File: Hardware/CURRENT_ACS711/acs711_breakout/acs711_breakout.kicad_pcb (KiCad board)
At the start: 2 copper layers, 40 x 30 mm, 13 parts, among them J1 Conn_01x01, J2 Conn_01x01, J3 Conn_01x04, U1 ACS711xEXLT-15AB

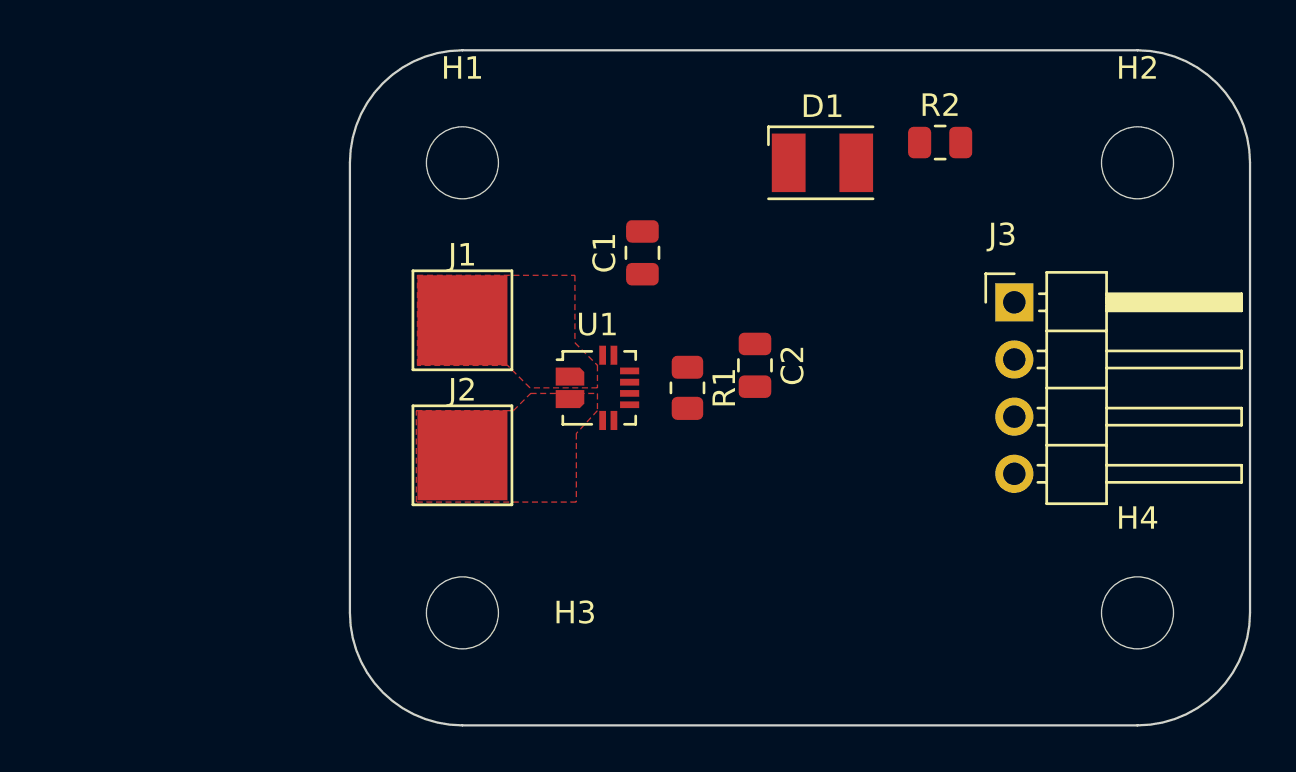
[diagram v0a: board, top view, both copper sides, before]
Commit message: layout and some stitching vias
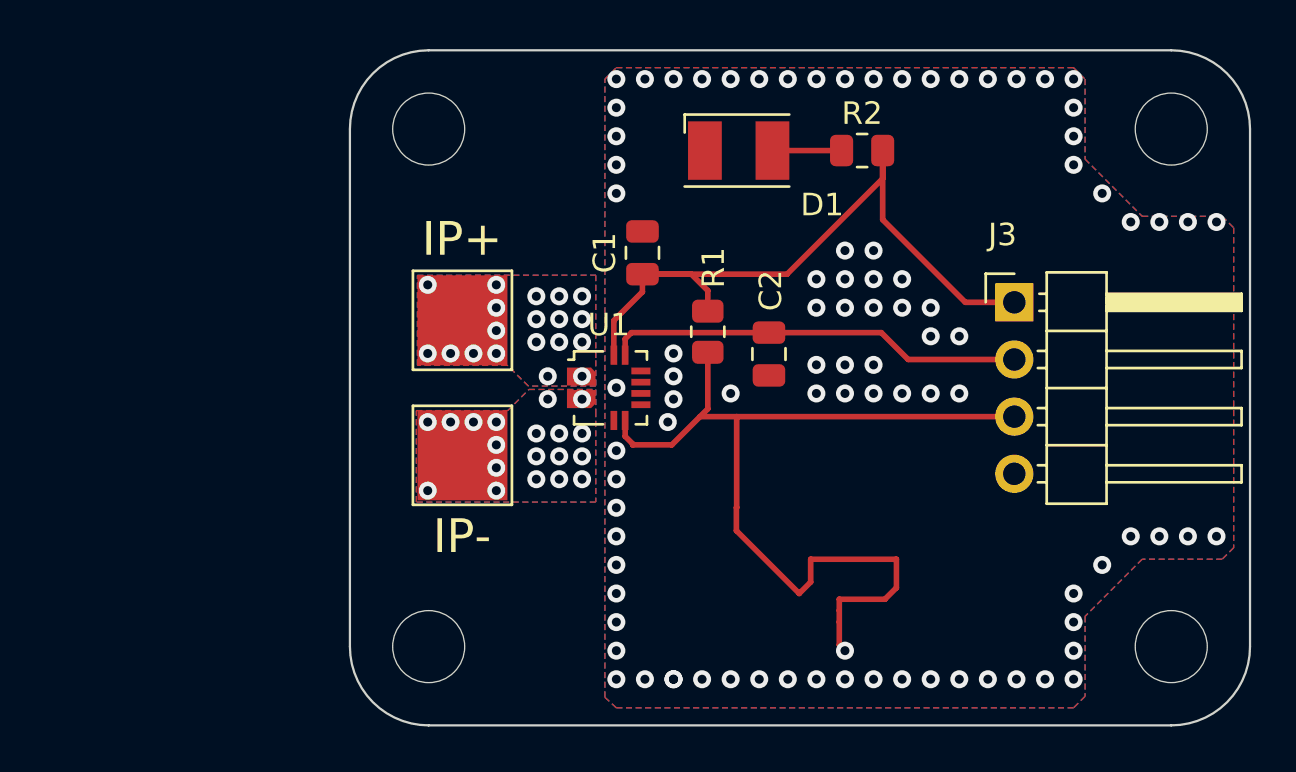
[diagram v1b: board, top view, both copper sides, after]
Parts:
- moved D1 3.76 mm to (122.3, 84.5)
- moved R2 3.49 mm to (127.8, 84.5)
- moved R1 2.65 mm to (120.9, 92.5)
- moved H1 2.12 mm to (108.5, 83.5)
- moved H2 2.12 mm to (141.5, 83.5)
- moved H3 2.12 mm to (108.5, 106.5)
- moved H4 2.12 mm to (141.5, 106.5)
- moved C2 0.80 mm to (123.6, 93.5)
- moved U1 0.50 mm to (116.5, 95.0)
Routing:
- net Net-(J3-Pad3): track 0.00 -> 42.7 mm, vias 0 -> 1
- net VCC: track 0.00 -> 32.4 mm
- net Net-(C2-Pad1): track 0.00 -> 18.6 mm
- net Net-(D1-Pad2): track 0.00 -> 3.07 mm
- net Net-(J2-Pad1): vias 0 -> 19
- net Net-(J1-Pad1): vias 0 -> 19
- net GND: vias 0 -> 91
- added copper zone on B.Cu, net GND
- added copper zone on F.Cu, net GND
- added copper zone on B.Cu, net Net-(J1-Pad1)
- added copper zone on B.Cu, net Net-(J2-Pad1)
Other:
- outline, holes or cut-outs redrawn
- board text added: "IP+"
- board text added: "IP-"

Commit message: Last version of altimeter and ACS7111 pcbs
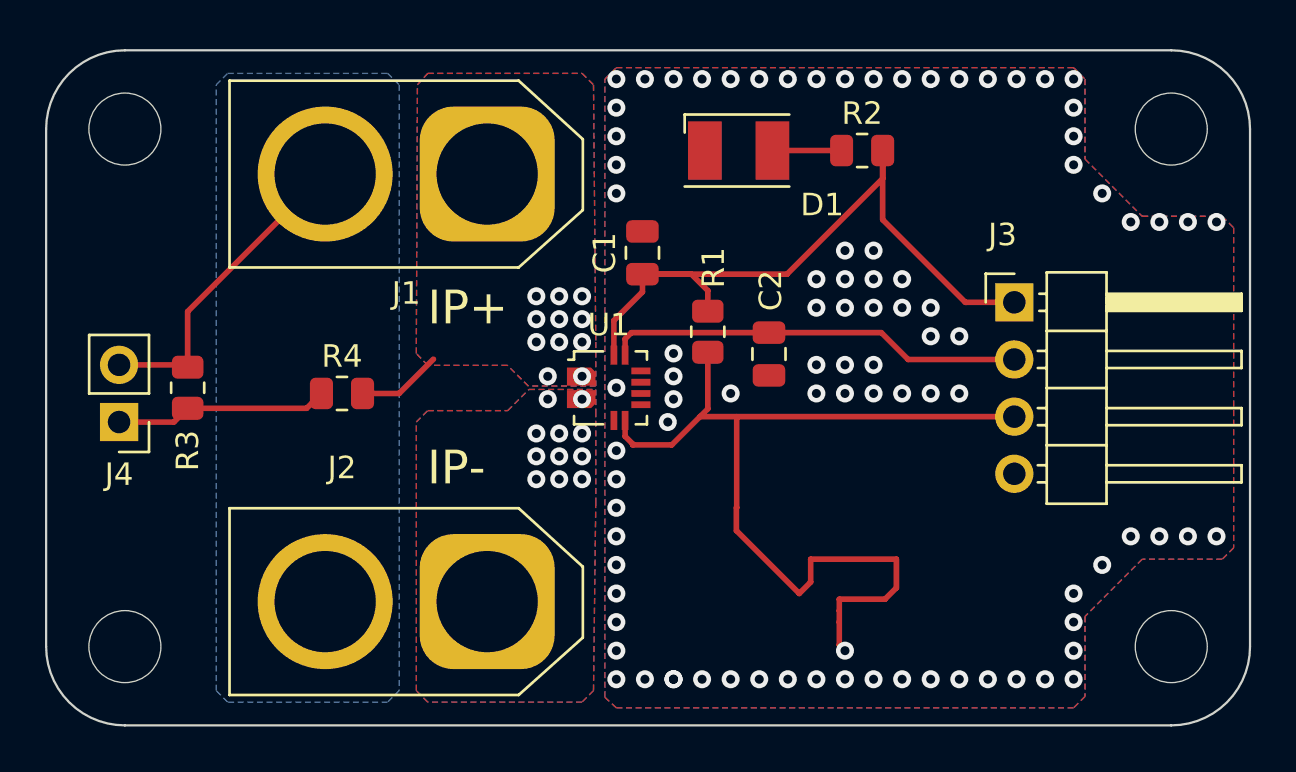
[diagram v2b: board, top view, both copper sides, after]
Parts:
- added J4: Conn_01x02, Connector_PinHeader_2.54mm:PinHeader_1x02_P2.54mm_Vertical, F.Cu at (94.7, 96.5)
- added R3: R_Small, Resistor_SMD:R_0805_2012Metric, F.Cu at (97.8, 95.0)
- added R4: R_Small, Resistor_SMD:R_0805_2012Metric, F.Cu at (104.6, 95.2)
- J1: value Conn_01x01 -> Conn_01x02; footprint TestPoint:TestPoint_Pad_4.0x4.0mm -> Connector_AMASS:AMASS_XT60-M_1x02_P7.20mm_Vertical
- J2: value Conn_01x01 -> Conn_01x02; footprint TestPoint:TestPoint_Pad_4.0x4.0mm -> Connector_AMASS:AMASS_XT60-F_1x02_P7.20mm_Vertical
- moved H1 13.5 mm to (95.0, 83.5)
- moved H3 13.5 mm to (95.0, 106.5)
- moved J1 6.59 mm to (111.1, 85.5), turned to 180 degrees
- moved J2 6.59 mm to (111.1, 104.5), turned to 180 degrees
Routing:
- net Net-(J1-Pad2): track 0.00 -> 14.2 mm
- net Net-(J4-Pad1): track 0.00 -> 9.52 mm
- net Net-(U1-Pad1): track 0.00 -> 3.78 mm, vias 19 -> 11
- net Net-(U1-Pad2): vias 19 -> 11
- added copper zone on B.Cu, net Net-(J1-Pad2)
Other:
- board size 40 x 30 mm -> 53.5 x 30 mm

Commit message: component update
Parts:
- C1: value C_Small -> 100nF
- C2: value C_Small -> DNP
- R1, R2: value R_Small -> 1k
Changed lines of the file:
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@@
       (effects (font (size 1 1) (thickness 0.15)))
     )
-    (fp_text value "R_Small" (at 0 1.65) (layer "F.Fab")
+    (fp_text value "1k" (at 0 1.65) (layer "F.Fab")
       (effects (font (size 1 1) (thickness 0.15)))
     )
@@
       (effects (font (size 1 1) (thickness 0.15)))
     )
-    (fp_text value "C_Small" (at 0 1.68 90) (layer "F.Fab")
+    (fp_text value "DNP" (at 0 1.68 90) (layer "F.Fab")
       (effects (font (size 1 1) (thickness 0.15)))
     )
@@
       (effects (font (size 1 1) (thickness 0.15)))
     )
-    (fp_text value "R_Small" (at 0 1.65 90) (layer "F.Fab")
+    (fp_text value "1k" (at 0 1.65 90) (layer "F.Fab")
       (effects (font (size 1 1) (thickness 0.15)))
     )
@@
       (effects (font (size 1 1) (thickness 0.15)))
     )
-    (fp_text value "C_Small" (at 0 1.68 90) (layer "F.Fab")
-      (effects (font (size 1 1) (thickness 0.15)))
-    )
+    (fp_text value "100nF" (at 0 1.68 90) (layer "F.Fab")
+      (effects (font (size 1 1) (thickness 0.15)))
+    )
